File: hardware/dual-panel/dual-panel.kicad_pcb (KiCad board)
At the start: 4 copper layers, 210.9 x 127 mm, 172 parts, among them J201 FSR West, J202 FSR South, J203 FSR East, J204 RS-485 IN, J205 12V_IN, J206 FSR North, J207 RS-485 OUT, J208 12V_OUT, J209 SWD, J210 Conn_01x08_Pin, J211 Conn_01x08_Pin, J212 Conn_01x08_Pin, J213 Conn_01x08_Pin, J214 INT OUT, J301 Conn_01x08_Socket, J302 Conn_01x08_Socket, J303 Conn_01x08_Socket, J304 Conn_01x08_Socket, J305 USB_C_Receptacle_USB2.0_16P, SW201 PANEL_ID, SW202 RS-485 Termination, SW301 BOOTSEL, U301 SN74AHCT1G125, U302 AP7361C-33ER-13, U303 AMS1117-5.0, U304 LM66200, U305 USBLC6-2SC6, U306 RP2040, U307 W25Q32JV, U308 THVD1429, X301 12MHz ABM8-272-T3

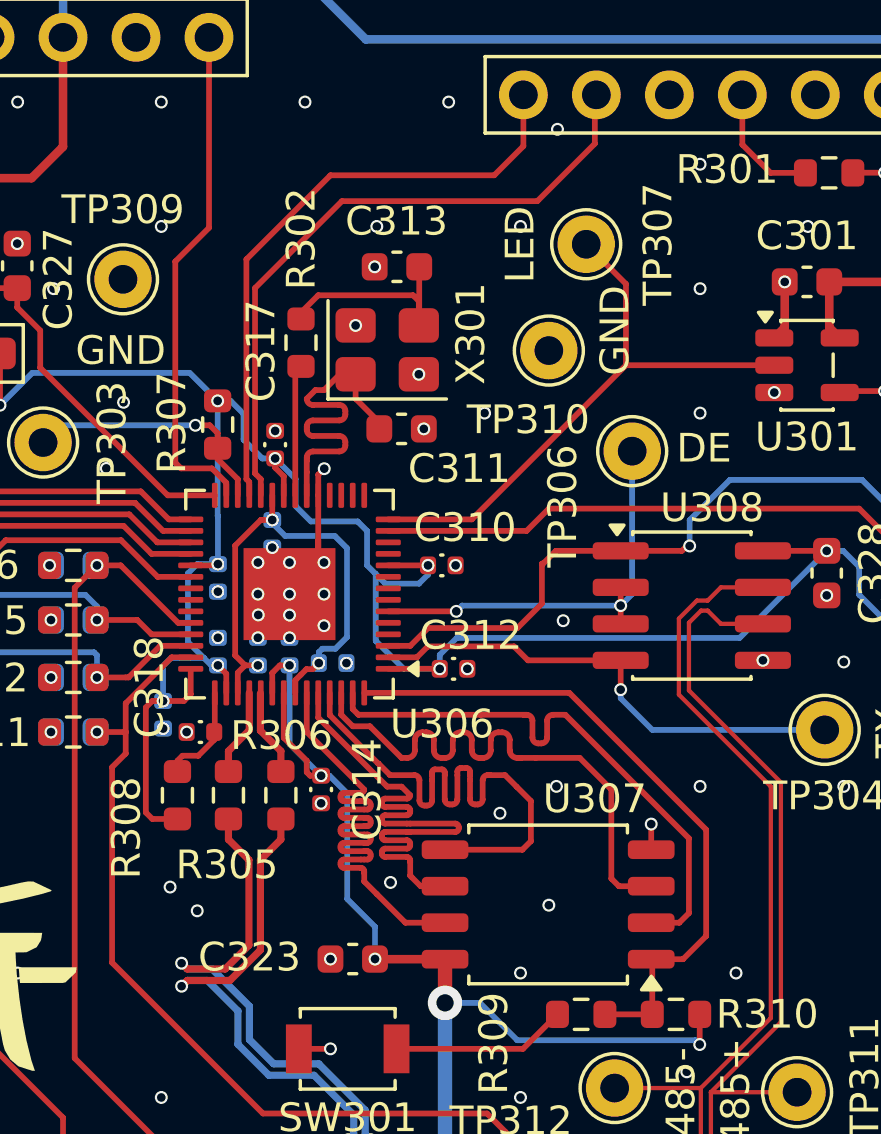
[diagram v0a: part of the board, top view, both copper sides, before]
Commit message: dual-panel: raise the clearance floor on the brain from 0.09mm to 0.127mm
The tightest copper on the board was 0.0900mm, sitting essentially on the
3.5mil standard-process limit with no margin. Two areas were responsible and
both are now opened up.

QSPI bus: the five data/clock nets escape the RP2040 at 0.400mm pitch, which
becomes 0.283mm perpendicular once a trace turns 45deg -- at 0.20mm width that
left ~0.09mm where SD0's diagonal passed SD2's turn corner. All QSPI traces
narrowed to 0.15mm, uniformly rather than necked locally so no impedance step
is introduced. Length matching was retuned in the process and is now held to a
20nm spread across the five matched nets (was 780nm).

SWD: SWDIO and SWCLK ran parallel for 6.45mm at 0.300mm pitch = 0.100mm gap.
Respaced to 0.400mm pitch. That initially pushed SWDIO into Net-(U306-RUN),
which was then resolved along with DEBUG_LED; the drag artifacts it left on
RUN (8.6um and 14.9um jogs) are gone.

Tightest clearance is now 0.1266mm (DEBUG_LED to Net-(U306-RUN)). Nothing
remains below 0.12mm. The USB+/USB- pair at 0.1375mm is a differential pair
and is deliberately coupled -- do not widen it.

Verified: DRC 0 violations, 19 unconnected (the cross-gap floor), ERC 0, zone
fill current, all 577 pads still match the exported netlist.
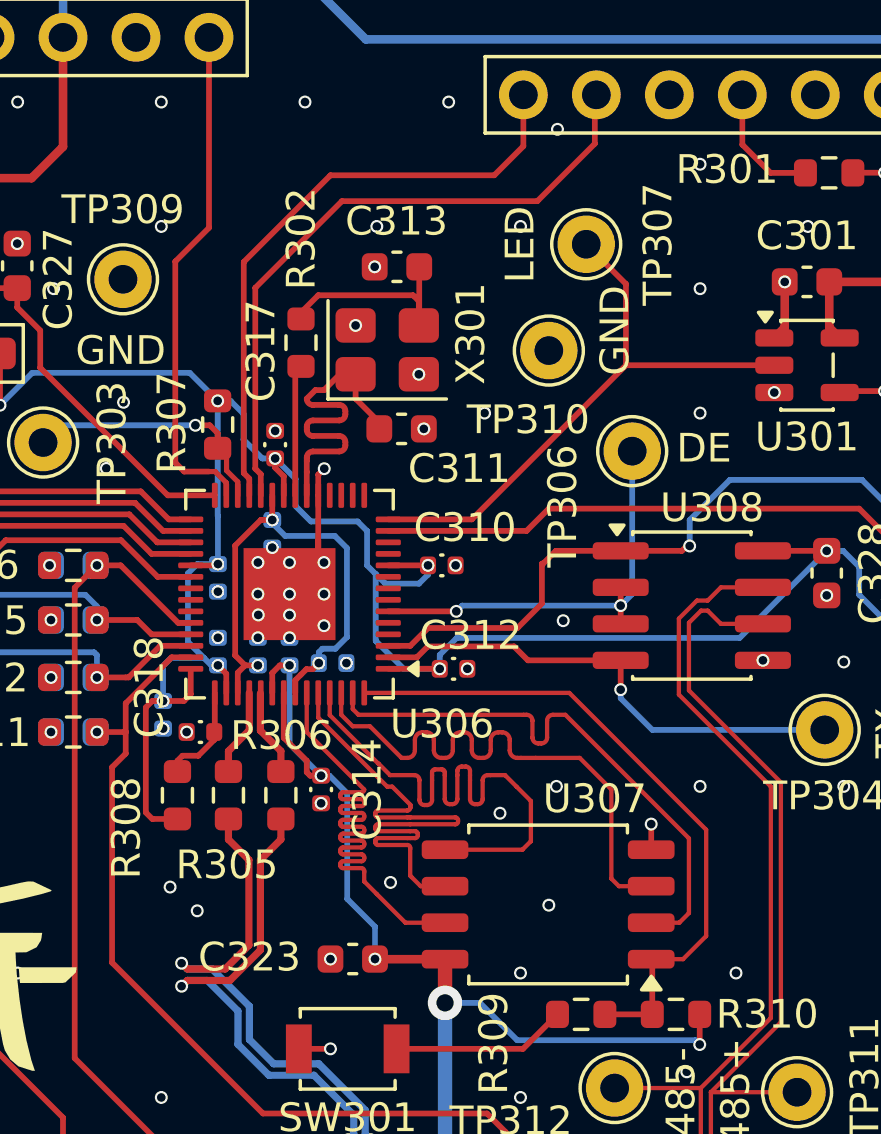
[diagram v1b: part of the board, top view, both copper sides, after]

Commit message: dual-panel: third mounting hole, fix hole refdes, set via fill/cap
Adds a third M3 fixing to both boards and moves the top one, which removes
the rocking degree of freedom the two-screw mount still had. With only two
screws the boards could rotate about the axis through them, and the two
board-to-board sockets furthest off that axis sat 27mm and 34mm out. Three
non-collinear fixings constrain the plane outright.

  arrangement                 worst socket-to-screw   support triangle
  2 screws (before)                   45.99 mm        none (collinear)
  old top + new bottom-right          41.46 mm        1576 mm2
  top moved + new bottom-right        32.07 mm        1583 mm2

Brain/carrier hole pairs stay on the exact (101.68, -16.87) offset.

Mounting hole refdes were swapped against the 2xx=carrier / 3xx=brain
convention: H201/H202 sat on the brain and H301/H302 on the carrier. The
schematic sheets were already right, so this swaps the footprint placements
only, leaving the symbol-to-footprint paths untouched. Their reference-text
offsets were swapped too, since those were tuned per location (a -0.81mm
nudge to clear J302's label, and one text placed below to stay off the
brain's top edge) and would otherwise have collided in their new homes.

Sets board-level via capping and filling ahead of ordering with JLC's epoxy
fill option. This is annotation only -- verified it changes nothing in the
Gerbers, drill, gerber job file, IPC-2581 or ODB++ output. Set at board level
rather than per-via because every via reads FROM_BOARD, and because the fill
is a whole-board process, not a per-via selection.

Also restores via tenting, which had been switched off. That opened a solder
mask window over all 1107 vias -- a bridging risk in assembly, and the cause
of 138 silkscreen-clipped-by-mask violations.

Stitching vias re-added after the clearance rework: 1107 total (1014 GND).
Carrier stitching matches the pre-rework board exactly (790 GND vias, median
GND-pad-to-via 1.55mm,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
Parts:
- added H203: MountingHole_Pad, MountingHole:MountingHole_3.2mm_M3_Pad, F.Cu at (146.0, 108.1)
- added H303: MountingHole_Pad, MountingHole:MountingHole_3.2mm_M3_Pad, F.Cu at (247.7, 91.2)
- moved H202 112.5 mm to (123.0, 53.9)
- moved H201 103.1 mm to (86.8, 106.2)
- moved H301 103.1 mm to (188.5, 89.3)
- moved H302 93.7 mm to (224.7, 37.0)
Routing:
- net TERM_SENSE: track 121.7 -> 125.5 mm
- net /carrier/LD4: track 75.0 -> 76.3 mm
- net /carrier/LD17: track 57.5 -> 58.6 mm
- net /carrier/LD16: track 69.1 -> 69.8 mm
- net GND: vias 991 -> 1014
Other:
- outline, holes or cut-outs redrawn
